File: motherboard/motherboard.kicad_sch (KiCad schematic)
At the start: 23 parts, among them J20 CM3588 Hirose Connector, J21 5V IN, J22 BATTERY IN, U26 AMS1117-1.8, U27 TPS54331DR

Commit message: motherboard net labeling and impedance matching
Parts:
- J21, J22: footprint Connector_Molex:Molex_PicoBlade_53398-1071_1x10-1MP_P1.25mm_Vertical -> Connector_Molex:Molex_PicoBlade_53261-1071_1x10-1MP_P1.25mm_Horizontal
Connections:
- net  GPIO3_C3/PWM15_IR_M0 renamed GPIO3_C3/PWM15_IR_M0
- net HDMI0_TX0N_PORT renamed HDMI0_TX0N
- net HDMI0_TX0P_PORT renamed HDMI0_TX0P
- net HDMI0_TX1N_PORT renamed HDMI0_TX1N
- net HDMI0_TX1P_PORT renamed HDMI0_TX1P
- net HDMI0_TX2N_PORT renamed HDMI0_TX2N
- net HDMI0_TX2P_PORT renamed HDMI0_TX2P
- net HDMI0_TX3N_PORT renamed HDMI0_TX3N
- net HDMI0_TX3P_PORT renamed HDMI0_TX3P
- net HDMI1_TX0N_PORT renamed HDMI1_TX0N
- net HDMI1_TX0P_PORT renamed HDMI1_TX0P
- net HDMI1_TX1N_PORT renamed HDMI1_TX1N
- net HDMI1_TX1P_PORT renamed HDMI1_TX1P
- net HDMI1_TX2N_PORT renamed HDMI1_TX2N
- net HDMI1_TX2P_PORT renamed HDMI1_TX2P
- net HDMI1_TX3N_PORT renamed HDMI1_TX3N
- net HDMI1_TX3P_PORT renamed HDMI1_TX3P
- net HDMI_RX_CLKN_PORT renamed HDMI_RX_CLKN
- net HDMI_RX_CLKP_PORT renamed HDMI_RX_CLKP
- net HDMI_RX_D0N_PORT renamed HDMI_RX_D0N
- net HDMI_RX_D0P_PORT renamed HDMI_RX_D0P
- net HDMI_RX_D1N_PORT renamed HDMI_RX_D1N
- net HDMI_RX_D1P_PORT renamed HDMI_RX_D1P
- net HDMI_RX_D2N_PORT renamed HDMI_RX_D2N
- net HDMI_RX_D2P_PORT renamed HDMI_RX_D2P
- net PCIE30_PORT0_REFCLKN_IN renamed PCIE30_PORT0_REFCLKN
- net PCIE30_PORT0_REFCLKP_IN renamed PCIE30_PORT0_REFCLKP
- net PCIE30_PORT1_REFCLKN_IN renamed PCIE30_PORT1_REFCLKN
- net PCIE30_PORT1_REFCLKP_IN renamed PCIE30_PORT1_REFCLKP
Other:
- sheet HDMI_TX ports: added HDMI0_TX0N, HDMI0_TX0P, HDMI0_TX1N, HDMI0_TX1P, HDMI0_TX2N, HDMI0_TX2P, HDMI0_TX3N, HDMI0_TX3P; removed HDMI0_TX0N_PORT, HDMI0_TX0P_PORT, HDMI0_TX1N_PORT, HDMI0_TX1P_PORT, HDMI0_TX2N_PORT, HDMI0_TX2P_PORT, HDMI0_TX3N_PORT, HDMI0_TX3P_PORT
- sheet PCIE3.0-MKEY ports: added PCIE0_PORT0_REFCLKN, PCIE0_PORT0_REFCLKP, PCIE0_PORT1_REFCLKN, PCIE0_PORT1_REFCLKP; removed PCIE0_PORT0_REFCLKN_IN, PCIE0_PORT0_REFCLKP_IN, PCIE0_PORT1_REFCLKN_IN, PCIE0_PORT1_REFCLKP_IN
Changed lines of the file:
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@@
 		)
 	)
-	(hierarchical_label "HDMI0_TX3P_PORT"
+	(hierarchical_label "HDMI0_TX3P"
 		(shape bidirectional)
 		(at 369.57 104.14 180)
@@
 		)
 	)
-	(hierarchical_label "HDMI0_TX1N_PORT"
+	(hierarchical_label "HDMI0_TX1N"
 		(shape bidirectional)
 		(at 71.12 234.95 180)
@@
 		)
 	)
-	(hierarchical_label "HDMI0_TX1P_PORT"
+	(hierarchical_label "HDMI0_TX1P"
 		(shape bidirectional)
 		(at 369.57 88.9 180)
@@
 		)
 	)
-	(hierarchical_label "HDMI0_TX2N_PORT"
+	(hierarchical_label "HDMI0_TX2N"
 		(shape bidirectional)
 		(at 71.12 241.3 180)
@@
 		)
 	)
-	(hierarchical_label "PCIE30_PORT0_REFCLKP_IN"
+	(hierarchical_label "PCIE30_PORT0_REFCLKP"
 		(shape input)
 		(at 283.21 58.42 0)
@@
 		)
 	)
-	(hierarchical_label "HDMI0_TX0N_PORT"
+	(hierarchical_label "HDMI0_TX0N"
 		(shape bidirectional)
 		(at 71.12 228.6 180)
@@
 		)
 	)
-	(hierarchical_label "HDMI1_TX3P_PORT"
+	(hierarchical_label "HDMI1_TX3P"
 		(shape output)
 		(at 254 250.19 180)
@@
 		)
 	)
-	(hierarchical_label "HDMI1_TX1P_PORT"
+	(hierarchical_label "HDMI1_TX1P"
 		(shape output)
 		(at 369.57 50.8 180)
@@
 		)
 	)
-	(hierarchical_label "HDMI1_TX3N_PORT"
+	(hierarchical_label "HDMI1_TX3N"
 		(shape output)
 		(at 369.57 68.58 180)
@@
 		)
 	)
-	(hierarchical_label "PCIE30_PORT0_REFCLKN_IN"
+	(hierarchical_label "PCIE30_PORT0_REFCLKN"
 		(shape input)
 		(at 321.31 294.64 180)
@@
 		)
 	)
-	(hierarchical_label "HDMI1_TX3P_PORT"
+	(hierarchical_label "HDMI1_TX3P"
 		(shape output)
 		(at 369.57 66.04 180)
@@
 		)
 	)
-	(hierarchical_label "HDMI1_TX0P_PORT"
+	(hierarchical_label "HDMI1_TX0P"
 		(shape output)
 		(at 369.57 58.42 180)
@@
 		)
 	)
-	(hierarchical_label "HDMI1_TX0N_PORT"
+	(hierarchical_label "HDMI1_TX0N"
 		(shape output)
 		(at 254 233.68 180)
@@
 		)
 	)
-	(hierarchical_label " GPIO3_C3{slash}PWM15_IR_M0"
+	(hierarchical_label "GPIO3_C3{slash}PWM15_IR_M0"
 		(shape output)
 		(at 245.11 157.48 180)
@@
 		)
 	)
-	(hierarchical_label "HDMI1_TX1P_PORT"
+	(hierarchical_label "HDMI1_TX1P"
 		(shape output)
 		(at 254 237.49 180)
@@
 		)
 	)
-	(hierarchical_label "HDMI0_TX1P_PORT"
+	(hierarchical_label "HDMI0_TX1P"
 		(shape bidirectional)
 		(at 71.12 232.41 180)
@@
 		)
 	)
-	(hierarchical_label "HDMI0_TX2N_PORT"
+	(hierarchical_label "HDMI0_TX2N"
 		(shape bidirectional)
 		(at 369.57 83.82 180)
@@
 		)
 	)
-	(hierarchical_label "HDMI_RX_D0P_PORT"
+	(hierarchical_label "HDMI_RX_D0P"
 		(shape bidirectional)
 		(at 407.67 88.9 0)
@@
 		)
 	)
-	(hierarchical_label "HDMI1_TX1N_PORT"
+	(hierarchical_label "HDMI1_TX1N"
 		(shape output)
 		(at 369.57 53.34 180)
@@
 		)
 	)
-	(hierarchical_label "HDMI1_TX0P_PORT"
+	(hierarchical_label "HDMI1_TX0P"
 		(shape output)
 		(at 254 231.14 180)
@@
 		)
 	)
-	(hierarchical_label "PCIE30_PORT1_REFCLKN_IN"
+	(hierarchical_label "PCIE30_PORT1_REFCLKN"
 		(shape input)
 		(at 375.92 294.64 0)
@@
 		)
 	)
-	(hierarchical_label "HDMI1_TX2P_PORT"
+	(hierarchical_label "HDMI1_TX2P"
 		(shape output)
 		(at 254 243.84 180)
@@
 		)
 	)
-	(hierarchical_label "PCIE30_PORT0_REFCLKP_IN"
+	(hierarchical_label "PCIE30_PORT0_REFCLKP"
 		(shape input)
 		(at 321.31 292.1 180)
@@
 		)
 	)
-	(hierarchical_label "HDMI0_TX0N_PORT"
+	(hierarchical_label "HDMI0_TX0N"
 		(shape bidirectional)
 		(at 369.57 99.06 180)
@@
 		)
 	)
-	(hierarchical_label "HDMI0_TX2P_PORT"
+	(hierarchical_label "HDMI0_TX2P"
 		(shape bidirectional)
 		(at 71.12 238.76 180)
@@
 		)
 	)
-	(hierarchical_label "HDMI_RX_D0N_PORT"
+	(hierarchical_label "HDMI_RX_D0N"
 		(shape bidirectional)
 		(at 407.67 91.44 0)
@@
 		)
 	)
-	(hierarchical_label "HDMI1_TX1N_PORT"
+	(hierarchical_label "HDMI1_TX1N"
 		(shape output)
 		(at 254 240.03 180)
@@
 		)
 	)
-	(hierarchical_label "PCIE30_PORT1_REFCLKN_IN"
+	(hierarchical_label "PCIE30_PORT1_REFCLKN"
 		(shape input)
 		(at 283.21 114.3 0)
@@
 		)
 	)
-	(hierarchical_label "HDMI_RX_D1N_PORT"
+	(hierarchical_label "HDMI_RX_D1N"
 		(shape bidirectional)
 		(at 407.67 83.82 0)
@@
 		)
 	)
-	(hierarchical_label "HDMI1_TX2N_PORT"
+	(hierarchical_label "HDMI1_TX2N"
 		(shape output)
 		(at 254 246.38 180)
@@
 		)
 	)
-	(hierarchical_label "HDMI0_TX0P_PORT"
+	(hierarchical_label "HDMI0_TX0P"
 		(shape bidirectional)
 		(at 369.57 96.52 180)
@@
 		)
 	)
-	(hierarchical_label "HDMI0_TX3N_PORT"
+	(hierarchical_label "HDMI0_TX3N"
 		(shape bidirectional)
 		(at 369.57 106.68 180)
@@
 		)
 	)
-	(hierarchical_label "HDMI_RX_D2P_PORT"
+	(hierarchical_label "HDMI_RX_D2P"
 		(shape bidirectional)
 		(at 407.67 73.66 0)
@@
 		)
 	)
-	(hierarchical_label "PCIE30_PORT0_REFCLKN_IN"
+	(hierarchical_label "PCIE30_PORT0_REFCLKN"
 		(shape input)
 		(at 283.21 60.96 0)
@@
 		)
 	)
-	(hierarchical_label "HDMI0_TX1N_PORT"
+	(hierarchical_label "HDMI0_TX1N"
 		(shape bidirectional)
 		(at 369.57 91.44 180)
@@
 		)
 	)
-	(hierarchical_label "HDMI1_TX3N_PORT"
+	(hierarchical_label "HDMI1_TX3N"
 		(shape output)
 		(at 254 252.73 180)
@@
 		)
 	)
-	(hierarchical_label "HDMI1_TX2N_PORT"
+	(hierarchical_label "HDMI1_TX2N"
 		(shape output)
 		(at 369.57 45.72 180)
@@
 		)
 	)
-	(hierarchical_label "PCIE30_PORT1_REFCLKP_IN"
+	(hierarchical_label "PCIE30_PORT1_REFCLKP"
 		(shape input)
 		(at 283.21 111.76 0)
@@
 		)
 	)
-	(hierarchical_label "HDMI1_TX2P_PORT"
+	(hierarchical_label "HDMI1_TX2P"
 		(shape output)
 		(at 369.57 43.18 180)
@@
 		)
 	)
-	(hierarchical_label "HDMI0_TX3P_PORT"
+	(hierarchical_label "HDMI0_TX3P"
 		(shape bidirectional)
 		(at 71.12 245.11 180)
@@
 		)
 	)
-	(hierarchical_label "HDMI0_TX0P_PORT"
+	(hierarchical_label "HDMI0_TX0P"
 		(shape bidirectional)
 		(at 71.12 226.06 180)
@@
 		)
 	)
-	(hierarchical_label "HDMI_RX_CLKN_PORT"
+	(hierarchical_label "HDMI_RX_CLKN"
 		(shape bidirectional)
 		(at 407.67 99.06 0)
@@
 		)
 	)
-	(hierarchical_label "PCIE30_PORT1_REFCLKP_IN"
+	(hierarchical_label "PCIE30_PORT1_REFCLKP"
 		(shape input)
 		(at 375.92 292.1 0)
@@
 		)
 	)
-	(hierarchical_label "HDMI0_TX3N_PORT"
+	(hierarchical_label "HDMI0_TX3N"
 		(shape bidirectional)
 		(at 71.12 247.65 180)
@@
 		)
 	)
-	(hierarchical_label "HDMI_RX_D2N_PORT"
+	(hierarchical_label "HDMI_RX_D2N"
 		(shape bidirectional)
 		(at 407.67 76.2 0)
@@
 		)
 	)
-	(hierarchical_label "HDMI1_TX0N_PORT"
+	(hierarchical_label "HDMI1_TX0N"
 		(shape output)
 		(at 369.57 60.96 180)
@@
 		)
 	)
-	(hierarchical_label "HDMI_RX_D1P_PORT"
+	(hierarchical_label "HDMI_RX_D1P"
 		(shape bidirectional)
 		(at 407.67 81.28 0)
@@
 		)
 	)
-	(hierarchical_label "HDMI0_TX2P_PORT"
+	(hierarchical_label "HDMI0_TX2P"
 		(shape bidirectional)
 		(at 369.57 81.28 180)
@@
 		)
 	)
-	(hierarchical_label "HDMI_RX_CLKP_PORT"
+	(hierarchical_label "HDMI_RX_CLKP"
 		(shape bidirectional)
 		(at 407.67 96.52 0)
@@
 			)
 		)
-		(property "Footprint" "Connector_Molex:Molex_PicoBlade_53398-1071_1x10-1MP_P1.25mm_Vertical"
+		(property "Footprint" "Connector_Molex:Molex_PicoBlade_53261-1071_1x10-1MP_P1.25mm_Horizontal"
 			(at 209.55 196.85 0)
 			(effects
@@
 			)
 		)
-		(property "Footprint" "Connector_Molex:Molex_PicoBlade_53398-1071_1x10-1MP_P1.25mm_Vertical"
+		(property "Footprint" "Connector_Molex:Molex_PicoBlade_53261-1071_1x10-1MP_P1.25mm_Horizontal"
 			(at 250.19 196.85 0)
 			(effects
@@
 			)
 		)
-		(pin "PCIE0_PORT1_REFCLKP_IN" input
+		(pin "PCIE0_PORT1_REFCLKP" input
 			(at 375.92 292.1 0)
 			(effects
@@
 			)
 		)
-		(pin "PCIE0_PORT0_REFCLKN_IN" input
+		(pin "PCIE0_PORT0_REFCLKN" input
 			(at 321.31 294.64 180)
 			(effects
@@
 			)
 		)
-		(pin "PCIE0_PORT0_REFCLKP_IN" input
+		(pin "PCIE0_PORT0_REFCLKP" input
 			(at 321.31 292.1 180)
 			(effects
@@
 			)
 		)
-		(pin "PCIE0_PORT1_REFCLKN_IN" input
+		(pin "PCIE0_PORT1_REFCLKN" input
 			(at 375.92 294.64 0)
 			(effects
@@
 			)
 		)
-		(pin "HDMI0_TX1N_PORT" bidirectional
+		(pin "HDMI0_TX1N" bidirectional
 			(at 71.12 234.95 180)
 			(effects
@@
 			)
 		)
-		(pin "HDMI0_TX0P_PORT" bidirectional
+		(pin "HDMI0_TX0P" bidirectional
 			(at 71.12 226.06 180)
 			(effects
@@
 			)
 		)
-		(pin "HDMI0_TX3N_PORT" bidirectional
+		(pin "HDMI0_TX3N" bidirectional
 			(at 71.12 247.65 180)
 			(effects
@@
 			)
 		)
-		(pin "HDMI0_TX3P_PORT" bidirectional
+		(pin "HDMI0_TX3P" bidirectional
 			(at 71.12 245.11 180)
 			(effects
@@
 			)
 		)
-		(pin "HDMI0_TX2P_PORT" bidirectional
+		(pin "HDMI0_TX2P" bidirectional
 			(at 71.12 238.76 180)
 			(effects
@@
 			)
 		)
-		(pin "HDMI0_TX2N_PORT" bidirectional
+		(pin "HDMI0_TX2N" bidirectional
 			(at 71.12 241.3 180)
 			(effects
@@
 			)
 		)
-		(pin "HDMI0_TX1P_PORT" bidirectional
+		(pin "HDMI0_TX1P" bidirectional
 			(at 71.12 232.41 180)
 			(effects
@@
 			)
 		)
-		(pin "HDMI0_TX0N_PORT" bidirectional
+		(pin "HDMI0_TX0N" bidirectional
 			(at 71.12 228.6 180)
 			(effects

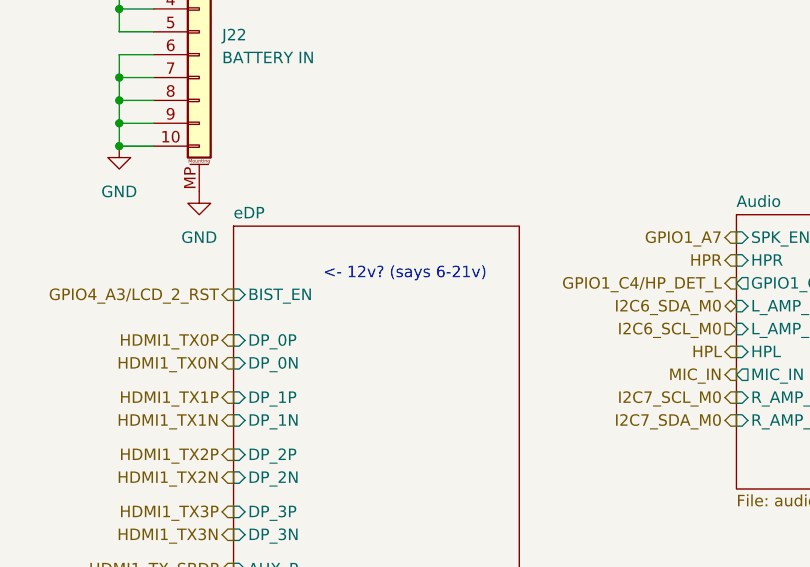
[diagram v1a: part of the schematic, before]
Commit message: starting motherboard v0.2
lessons from display eval v1
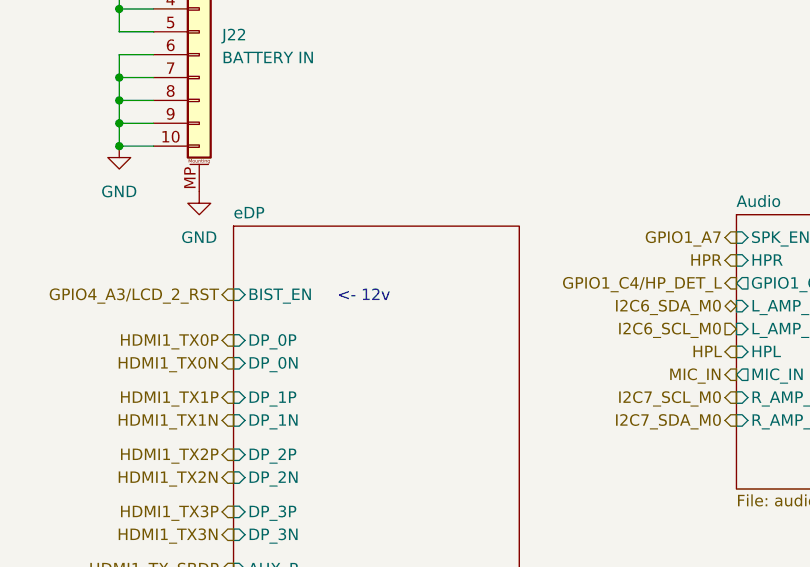
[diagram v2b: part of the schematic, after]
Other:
- note added: "<- 12v"
- note removed: "<- 12v? (says 6-21v)"
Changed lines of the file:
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@@
 		)
 	)
-	(text "<- 12v? (says 6-21v)"
+	(text "<- 12v"
 		(exclude_from_sim no)
-		(at 273.05 223.774 0)
+		(at 268.478 226.314 0)
 		(effects
 			(font

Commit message: v0.2 layout
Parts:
- removed C82: 100nF, Capacitor_SMD:C_0402_1005Metric, symbol Device:C_Small
- removed C83, C87, C88, C92, C93: 10uF, Capacitor_SMD:C_0603_1608Metric, symbol Device:C_Small
- removed C84: 1uF, Capacitor_SMD:C_0402_1005Metric, symbol Device:C_Small
- removed C85: 1nF, Capacitor_SMD:C_0402_1005Metric, symbol Device:C_Small
- removed C86: 10pF, Capacitor_SMD:C_0402_1005Metric, symbol Device:C_Small
- removed C89: 8.2nF, Capacitor_SMD:C_0402_1005Metric, symbol Device:C_Small
- removed D8: SS54, Diode_SMD:D_SMA, symbol Device:D_Schottky
- removed J21: 5V IN, Connector_Molex:Molex_PicoBlade_53261-1071_1x10-1MP_P1.25mm_Horizontal, symbol Connector_Generic_MountingPin:Conn_01x10_MountingPin
- removed R112: 24k, Resistor_SMD:R_0402_1005Metric, symbol Device:R_Small
- removed R113: 2k, Resistor_SMD:R_0402_1005Metric, symbol Device:R_Small
- removed R114: 10k, Resistor_SMD:R_0402_1005Metric, symbol Device:R_Small
- removed R115: 3.3k, Resistor_SMD:R_0402_1005Metric, symbol Device:R_Small
- removed U27: TPS54331DR, TPS54331DR:SOIC127P599X175-8N, symbol TPS54331DR:TPS54331DR
- added C39, C41, C43, C44, C49, C51, C52, C74, C75: 22uF, Capacitor_SMD:C_0603_1608Metric, symbol Device:C_Small
- added C40, C42, C50, C53, C70, C76: 100nF, Capacitor_SMD:C_0402_1005Metric, symbol Device:C_Small
- added L1, L3: MWSA0603S-3R3MT, Inductor_SMD:L_Sunlord_MWSA0603S, symbol Device:L_Small
- added R12, R16, R54, R6, R7: 10k, Resistor_SMD:R_0402_1005Metric, symbol Device:R_Small
- added R13: 220k, Resistor_SMD:R_0402_1005Metric, symbol Device:R_Small
- added R14: 33k, Resistor_SMD:R_0402_1005Metric, symbol Device:R_Small
- added R15: 330k, Resistor_SMD:R_0402_1005Metric, symbol Device:R_Small
- added R17, R8: 49.9k, Resistor_SMD:R_0402_1005Metric, symbol Device:R_Small
- added R53, R9: 510k, Resistor_SMD:R_0402_1005Metric, symbol Device:R_Small
- added U17, U20, U23: TPS564257DRLR, TPS564257:SOT50P160X60-6N, symbol TPS564257:TPS564257DRLR
- L2: value 3.3uH -> FXL0630-4R7-M; footprint Inductor_SMD:L_Vishay_IHLP-1616 -> Inductor_SMD:L_Sunlord_MWSA0603S
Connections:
- net +3.3V: now also C80.1, U26.3 (VI), C41.1, C42.1, C43.1, L3.2, R6.2; no longer L2.1
- net +5V: now also L2.2, C74.1, C75.1, C76.1, R12.2; no longer C80.1, U26.3 (VI)
- net GND: now also C39.2, C40.2, C41.2, C42.2, C43.2, C44.2, C49.2, C50.2, C51.2, C52.2, C53.2, C70.2, C74.2, C75.2, C76.2, R14.1, R15.1, R54.1, R7.1, U17.3 (GND), U20.3 (GND), U23.3 (GND)
- net PMIC_EXT_EN_OUT: now also U17.5 (EN), U20.5 (EN), U23.5 (EN)
- net VDD: now also C39.1, C40.1, C44.1, C49.1, C50.1, C70.1, U17.1 (VIN), U20.1 (VIN), U23.1 (VIN)
- net GPIO0_C6/PW M5_M1 renamed GPIO0_C6/PWM5_M1
- new net: L2.1, U23.2 (SW)
- new net: R12.1, U23.4 (PG)
- new net: R13.2, U23.6 (FB)
- new net: R13.1, R14.2, R15.2
- new net: R17.1, R53.1, R54.2
- new net: R17.2, R53.2, U20.6 (FB)
- new net: L1.1, U20.2 (SW)
- new net: R16.1, U20.4 (PG)
- new net: R7.2, R8.1, R9.1
- new net: R8.2, R9.2, U17.6 (FB)
- new net: R6.1, U17.4 (PG)
- new net: L3.1, U17.2 (SW)
- new net +3.3V_PCIE: C51.1, C52.1, C53.1, L1.2, R16.2
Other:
- moved on the sheet: C80, C81, J22, U26

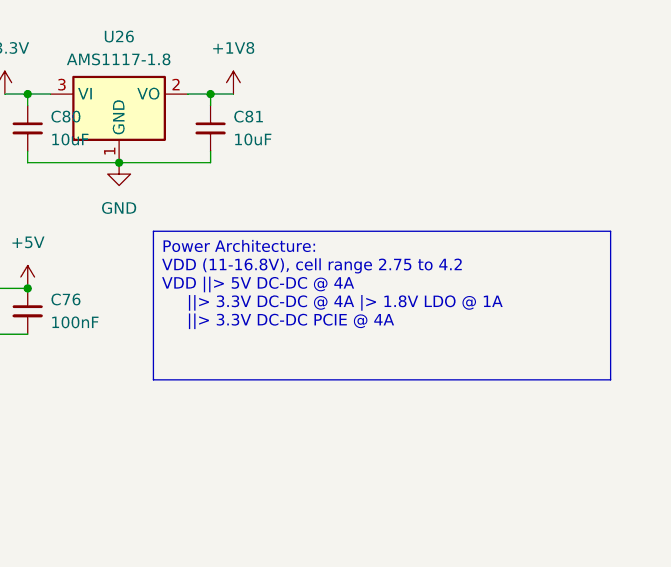
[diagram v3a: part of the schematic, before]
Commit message: 6 layer for better high speed signaling integrity
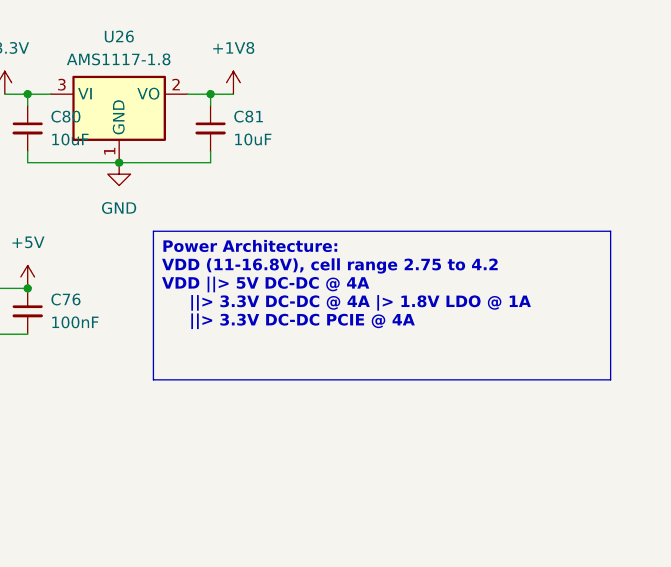
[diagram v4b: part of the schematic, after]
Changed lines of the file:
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@@
 				(face "JetBrains Mono")
 				(size 1.27 1.27)
+				(thickness 0.254)
+				(bold yes)
 			)
 			(justify left top)

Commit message: v0.2 good routing checkpoint (217 unrouted)
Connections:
- net USB20_HOST0_DM renamed USB20_HOST0_DN
- net USB20_HOST1_DM renamed USB20_HOST1_DN
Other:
- sheet Audio ports: added AMP_SCL, AMP_SDA; removed L_AMP_SCL, L_AMP_SDA, R_AMP_SCL, R_AMP_SDA
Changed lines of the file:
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@@
 		)
 	)
-	(hierarchical_label "USB20_HOST1_DM"
+	(hierarchical_label "USB20_HOST1_DN"
 		(shape bidirectional)
 		(at 60.96 299.72 180)
@@
 		)
 	)
-	(hierarchical_label "USB20_HOST1_DM"
+	(hierarchical_label "USB20_HOST1_DN"
 		(shape bidirectional)
 		(at 407.67 60.96 0)
@@
 		)
 	)
-	(hierarchical_label "I2C7_SDA_M0"
-		(shape output)
-		(at 300.99 214.63 180)
-		(fields_autoplaced yes)
-		(effects
-			(font
-				(size 1.27 1.27)
-			)
-			(justify right)
-		)
-	)
 	(hierarchical_label "GPIO3_B4"
 		(shape output)
@@
 		)
 	)
-	(hierarchical_label "USB20_HOST0_DM"
+	(hierarchical_label "USB20_HOST0_DN"
 		(shape bidirectional)
 		(at 407.67 68.58 0)
@@
 		)
 	)
-	(hierarchical_label "I2C7_SCL_M0"
-		(shape output)
-		(at 300.99 212.09 180)
-		(fields_autoplaced yes)
-		(effects
-			(font
-				(size 1.27 1.27)
-			)
-			(justify right)
-		)
-	)
 	(hierarchical_label "HDMI_RX_CEC"
 		(shape bidirectional)
@@
 		)
 	)
-	(hierarchical_label "USB20_HOST0_DM"
+	(hierarchical_label "USB20_HOST0_DN"
 		(shape bidirectional)
 		(at 304.8 294.64 180)
@@
 			)
 		)
-		(pin "L_AMP_SDA" input
-			(at 300.99 201.93 180)
-			(effects
-				(font
-					(size 1.27 1.27)
-				)
-				(justify left)
-			)
-		)
-		(pin "L_AMP_SCL" input
-			(at 300.99 204.47 180)
-			(effects
-				(font
-					(size 1.27 1.27)
-				)
-				(justify left)
-			)
-		)
 		(pin "HPL" input
 			(at 300.99 207.01 180)
@@
 			)
 		)
-		(pin "R_AMP_SCL" input
-			(at 300.99 212.09 180)
+		(pin "AMP_SCL" input
+			(at 300.99 204.47 180)
 			(effects
 				(font
@@
 			)
 		)
-		(pin "R_AMP_SDA" input
-			(at 300.99 214.63 180)
+		(pin "AMP_SDA" input
+			(at 300.99 201.93 180)
 			(effects
 				(font

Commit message: v0.2 75 routes left!
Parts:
- removed C80, C81: 10uF, Capacitor_SMD:C_0603_1608Metric, symbol Device:C_Small
- removed U26: AMS1117-1.8, Package_TO_SOT_SMD:SOT-223-3_TabPin2, symbol Regulator_Linear:AMS1117-1.8
- added C69, C77: 1uF, Capacitor_SMD:C_0402_1005Metric, symbol Device:C_Small
- added U24: RT9193-18GB, Package_TO_SOT_SMD:SOT-23-5, symbol RT9193-18GB:RT9193-18GB
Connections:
- net +1V8: now also C77.1, U24.5 (VOUT)
- net +3.3V: now also C69.1, U24.1 (VIN), U24.3 (EN)
- net GND: now also C69.2, C77.2, U24.2 (GND)
- net 5V_SW: now reaches L2.1, U23.2 (SW)
- net PCIE_SW: now reaches L1.1, U20.2 (SW)
- net 3V3_SW: now reaches L3.1, U17.2 (SW)
- no-connect marks 66 -> 67
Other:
- moved on the sheet: C41, C42, C43, C51, C52, C53, C74, C75, C76, L1, L2, L3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
